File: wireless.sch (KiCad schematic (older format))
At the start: 18 parts, among them U7 NRF24L01+, X2 16MHz 10ppm

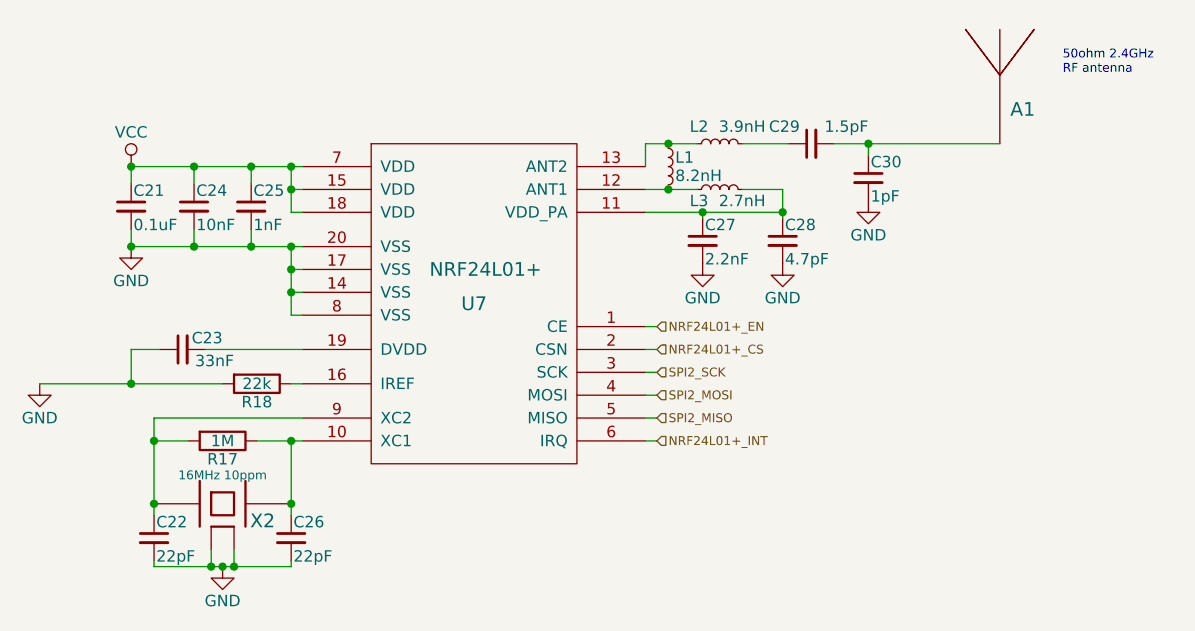
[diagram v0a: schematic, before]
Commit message: Fix problems noted by @nuft during review
- Force pulldown on unused bootloadr pins (USART 1 & 3)
- Use one oscillator for both MCU and NRF
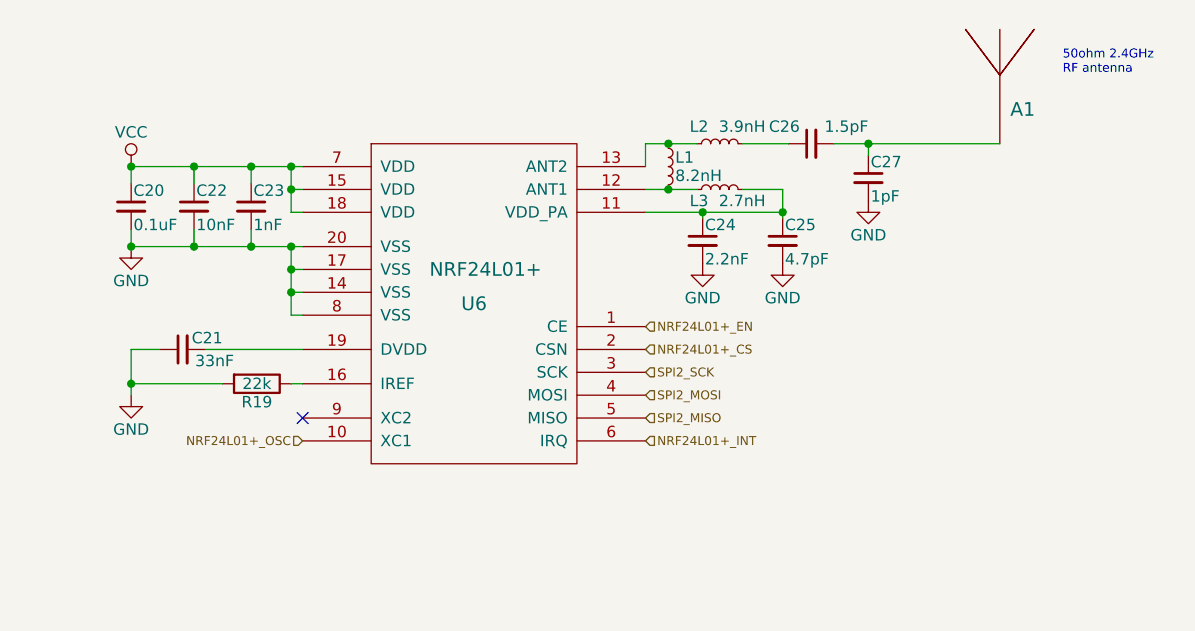
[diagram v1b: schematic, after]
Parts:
- removed C22, C26: 22pF, _std:_0402, symbol C_Small
- removed R17: 1M, _std:_0402, symbol R
- removed X2: 16MHz 10ppm, _div:_TSX-3225-SMD-XTAL, symbol XTAL-SMD-4-PADS
- renumbered C21 to C20, C23 to C21, C24 to C22, C25 to C23, C27 to C24, C28 to C25, C29 to C26, C30 to C27, R18 to R19, U7 to U6
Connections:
- net NRF24L01+_OSC: now reaches U6.10 (XC1)
- no-connect marks 0 -> 1
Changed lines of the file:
@@
 Sheet 3 4
 Title "Speedy the nanocopter"
-Date "2016-02-01"
+Date "2016-02-19"
 Rev "1C"
 Comp "Salah-Eddine Missri"
@@
 $EndDescr
 $Comp
-L NRF24R01+ U7
+L NRF24R01+ U6
 U 1 1 55438B0D
 P 5175 3125
-F 0 "U7" H 5175 3125 60  0000 C CNN
+F 0 "U6" H 5175 3125 60  0000 C CNN
 F 1 "NRF24L01+" H 5225 3275 60  0000 C CNN
 F 2 "Housings_DFN_QFN:QFN-20-1EP_4x4mm_Pitch0.5mm" H 5175 3125 60  0001 C CNN
@@
 $EndComp
 $Comp
-L VCC #PWR041
+L VCC #PWR036
 U 1 1 55438B1A
 P 3675 2525
-F 0 "#PWR041" H 3675 2375 50  0001 C CNN
+F 0 "#PWR036" H 3675 2375 50  0001 C CNN
 F 1 "VCC" H 3675 2675 50  0000 C CNN
 F 2 "" H 3675 2525 60  0000 C CNN
@@
 $EndComp
 $Comp
-L GND #PWR042
+L GND #PWR037
 U 1 1 55438B20
-P 3275 3475
-F 0 "#PWR042" H 3275 3225 50  0001 C CNN
-F 1 "GND" H 3275 3325 50  0000 C CNN
-F 2 "" H 3275 3475 60  0000 C CNN
-F 3 "" H 3275 3475 60  0000 C CNN
-	1    3275 3475
-	1    0    0    -1
-$EndComp
-$Comp
-L R R18
+P 3675 3525
+F 0 "#PWR037" H 3675 3275 50  0001 C CNN
+F 1 "GND" H 3675 3375 50  0000 C CNN
+F 2 "" H 3675 3525 60  0000 C CNN
+F 3 "" H 3675 3525 60  0000 C CNN
+	1    3675 3525
+	1    0    0    -1
+$EndComp
+$Comp
+L R R19
 U 1 1 55438B26
 P 4225 3475
-F 0 "R18" V 4305 3475 50  0000 C CNN
+F 0 "R19" V 4305 3475 50  0000 C CNN
 F 1 "22k" V 4225 3475 50  0000 C CNN
 F 2 "_std:_0402" V 4155 3475 30  0001 C CNN
@@
 $EndComp
 $Comp
-L GND #PWR043
-U 1 1 55438B2D
-P 4075 4275
-F 0 "#PWR043" H 4075 4025 50  0001 C CNN
-F 1 "GND" H 4075 4125 50  0000 C CNN
-F 2 "" H 4075 4275 60  0000 C CNN
-F 3 "" H 4075 4275 60  0000 C CNN
-	1    4075 4275
-	1    0    0    -1
-$EndComp
-$Comp
-L GND #PWR044
+L GND #PWR038
 U 1 1 55438B33
 P 6175 2950
-F 0 "#PWR044" H 6175 2700 50  0001 C CNN
+F 0 "#PWR038" H 6175 2700 50  0001 C CNN
 F 1 "GND" H 6175 2800 50  0000 C CNN
 F 2 "" H 6175 2950 60  0000 C CNN
@@
 $EndComp
 $Comp
-L GND #PWR045
+L GND #PWR039
 U 1 1 55438B39
 P 6525 2950
-F 0 "#PWR045" H 6525 2700 50  0001 C CNN
+F 0 "#PWR039" H 6525 2700 50  0001 C CNN
 F 1 "GND" H 6525 2800 50  0000 C CNN
 F 2 "" H 6525 2950 60  0000 C CNN
@@
 $EndComp
 $Comp
-L C_Small C29
+L C_Small C26
 U 1 1 55438B54
 P 6650 2425
-F 0 "C29" V 6725 2475 50  0000 L CNN
+F 0 "C26" V 6725 2475 50  0000 L CNN
 F 1 "1.5pF" V 6725 2175 50  0000 L CNN
 F 2 "_std:_0402" H 6650 2425 60  0001 C CNN
@@
 $EndComp
 $Comp
-L GND #PWR046
+L GND #PWR040
 U 1 1 55438B5B
 P 6900 2675
-F 0 "#PWR046" H 6900 2425 50  0001 C CNN
+F 0 "#PWR040" H 6900 2425 50  0001 C CNN
 F 1 "GND" H 6900 2525 50  0000 C CNN
 F 2 "" H 6900 2675 60  0000 C CNN
@@
 $EndComp
 $Comp
-L C_Small C27
+L C_Small C24
 U 1 1 55438B61
 P 6175 2850
-F 0 "C27" H 6185 2920 50  0000 L CNN
+F 0 "C24" H 6185 2920 50  0000 L CNN
 F 1 "2.2nF" H 6185 2770 50  0000 L CNN
 F 2 "_std:_0402" H 6175 2850 60  0001 C CNN
@@
 $EndComp
 $Comp
-L C_Small C28
+L C_Small C25
 U 1 1 55438B68
 P 6525 2850
-F 0 "C28" H 6535 2920 50  0000 L CNN
+F 0 "C25" H 6535 2920 50  0000 L CNN
 F 1 "4.7pF" H 6535 2770 50  0000 L CNN
 F 2 "_std:_0402" H 6525 2850 60  0001 C CNN
@@
 $EndComp
 $Comp
-L R R17
-U 1 1 55438B76
-P 4075 3725
-F 0 "R17" V 4155 3725 50  0000 C CNN
-F 1 "1M" V 4075 3725 50  0000 C CNN
-F 2 "_std:_0402" V 4005 3725 30  0001 C CNN
-F 3 "" H 4075 3725 30  0000 C CNN
-	1    4075 3725
-	0    1    1    0
-$EndComp
-$Comp
-L C_Small C22
-U 1 1 55438B7D
-P 3775 4150
-F 0 "C22" H 3785 4220 50  0000 L CNN
-F 1 "22pF" H 3785 4070 50  0000 L CNN
-F 2 "_std:_0402" H 3775 4150 60  0001 C CNN
-F 3 "" H 3775 4150 60  0000 C CNN
-	1    3775 4150
-	1    0    0    -1
-$EndComp
-$Comp
-L C_Small C26
-U 1 1 55438B84
-P 4375 4150
-F 0 "C26" H 4385 4220 50  0000 L CNN
-F 1 "22pF" H 4385 4070 50  0000 L CNN
-F 2 "_std:_0402" H 4375 4150 60  0001 C CNN
-F 3 "" H 4375 4150 60  0000 C CNN
-	1    4375 4150
-	1    0    0    -1
-$EndComp
-$Comp
-L C_Small C23
+L C_Small C21
 U 1 1 55438B8B
 P 3900 3325
-F 0 "C23" V 3950 3150 50  0000 L CNN
+F 0 "C21" V 3950 3150 50  0000 L CNN
 F 1 "33nF" V 3850 3100 50  0000 L CNN
 F 2 "_std:_0402" H 3900 3325 60  0001 C CNN
@@
 $EndComp
 $Comp
-L C_Small C30
+L C_Small C27
 U 1 1 55438B92
 P 6900 2575
-F 0 "C30" H 6910 2645 50  0000 L CNN
+F 0 "C27" H 6910 2645 50  0000 L CNN
 F 1 "1pF" H 6910 2495 50  0000 L CNN
 F 2 "_std:_0402" H 6900 2575 60  0001 C CNN
@@
 $EndComp
 $Comp
-L C_Small C21
+L C_Small C20
 U 1 1 55438B99
 P 3675 2700
-F 0 "C21" H 3685 2770 50  0000 L CNN
+F 0 "C20" H 3685 2770 50  0000 L CNN
 F 1 "0.1uF" H 3685 2620 50  0000 L CNN
 F 2 "_std:_0402" H 3675 2700 60  0001 C CNN
@@
 $EndComp
 $Comp
-L C_Small C25
+L C_Small C23
 U 1 1 55438BA0
 P 4200 2700
-F 0 "C25" H 4210 2770 50  0000 L CNN
+F 0 "C23" H 4210 2770 50  0000 L CNN
 F 1 "1nF" H 4210 2620 50  0000 L CNN
 F 2 "_std:_0402" H 4200 2700 60  0001 C CNN
@@
 $EndComp
 $Comp
-L GND #PWR047
+L GND #PWR041
 U 1 1 55438BA7
 P 3675 2875
-F 0 "#PWR047" H 3675 2625 50  0001 C CNN
+F 0 "#PWR041" H 3675 2625 50  0001 C CNN
 F 1 "GND" H 3675 2725 50  0000 C CNN
 F 2 "" H 3675 2875 60  0000 C CNN
@@
 	1    0    0    -1
 $EndComp
-Connection ~ 4075 4275
-Wire Wire Line
-	3775 4275 4375 4275
-Connection ~ 3775 4000
-Connection ~ 4375 4000
-Connection ~ 4375 3725
-Connection ~ 3775 3725
-Wire Wire Line
-	3925 3725 3775 3725
 Connection ~ 3675 3475
 Wire Wire Line
-	3275 3475 4075 3475
-Wire Wire Line
-	4425 3475 4375 3475
+	3675 3325 3675 3525
+Wire Wire Line
+	3675 3475 4075 3475
 Wire Wire Line
 	3675 3325 3800 3325
@@
 Wire Wire Line
 	3675 2800 3675 2875
-Wire Wire Line
-	3675 3325 3675 3475
 Connection ~ 4200 2525
 Wire Wire Line
@@
 Wire Wire Line
 	3675 2875 4425 2875
-Wire Wire Line
-	3775 3625 3775 4050
-Wire Wire Line
-	4425 3625 3775 3625
-Wire Wire Line
-	4375 3725 4375 4050
-Wire Wire Line
-	4225 3725 4425 3725
-Wire Wire Line
-	5975 3725 5925 3725
-Wire Wire Line
-	5975 3225 5925 3225
-Wire Wire Line
-	5925 3625 5975 3625
-Wire Wire Line
-	5975 3525 5925 3525
-Wire Wire Line
-	5925 3425 5975 3425
-Wire Wire Line
-	5975 3325 5925 3325
 Wire Wire Line
 	6525 2625 6525 2750
@@
 Connection ~ 6025 2425
 Connection ~ 6025 2625
-Wire Wire Line
-	3775 4250 3775 4275
-Wire Wire Line
-	4375 4275 4375 4250
 Connection ~ 3675 2875
 Connection ~ 4375 2875
@@
 Connection ~ 4200 2875
 $Comp
-L C_Small C24
+L C_Small C22
 U 1 1 55438BFC
 P 3950 2700
-F 0 "C24" H 3960 2770 50  0000 L CNN
+F 0 "C22" H 3960 2770 50  0000 L CNN
 F 1 "10nF" H 3960 2620 50  0000 L CNN
 F 2 "_std:_0402" H 3950 2700 60  0001 C CNN
@@
 Text Notes 7750 2125 0    39   ~ 0
 50ohm 2.4GHz\nRF antenna
-Text HLabel 5975 3225 2    39   Input ~ 0
+Text HLabel 5925 3225 2    39   Input ~ 0
 NRF24L01+_EN
-Text HLabel 5975 3325 2    39   Input ~ 0
+Text HLabel 5925 3325 2    39   Input ~ 0
 NRF24L01+_CS
-Text HLabel 5975 3425 2    39   Input ~ 0
+Text HLabel 5925 3425 2    39   Input ~ 0
 SPI2_SCK
-Text HLabel 5975 3525 2    39   Input ~ 0
+Text HLabel 5925 3525 2    39   Input ~ 0
 SPI2_MOSI
-Text HLabel 5975 3625 2    39   Input ~ 0
+Text HLabel 5925 3625 2    39   Input ~ 0
 SPI2_MISO
-Text HLabel 5975 3725 2    39   Input ~ 0
+Text HLabel 5925 3725 2    39   Input ~ 0
 NRF24L01+_INT
-$Comp
-L XTAL-SMD-4-PADS X2
-U 1 1 558EB9B5
-P 4075 4000
-F 0 "X2" H 4250 3925 60  0000 C CNN
-F 1 "16MHz 10ppm" H 4075 4125 39  0000 C CNN
-F 2 "_div:_TSX-3225-SMD-XTAL" H 4075 4000 60  0001 C CNN
-F 3 "" H 4075 4000 60  0000 C CNN
-	1    4075 4000
-	1    0    0    -1
-$EndComp
-Wire Wire Line
-	4025 4200 4025 4275
-Connection ~ 4025 4275
-Wire Wire Line
-	4125 4200 4125 4275
-Connection ~ 4125 4275
+NoConn ~ 4425 3625
+Text HLabel 4425 3725 0    39   Input ~ 0
+NRF24L01+_OSC
+Wire Wire Line
+	4425 3475 4375 3475
 $EndSCHEMATC

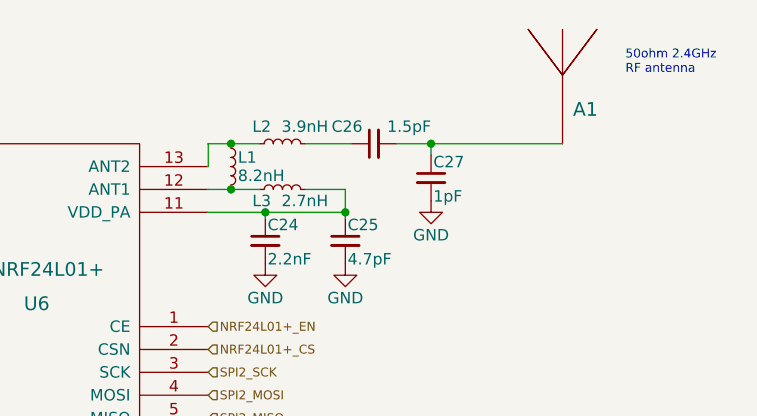
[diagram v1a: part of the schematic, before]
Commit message: Update TOF sensor to use new ST VL53L0X with 2m range
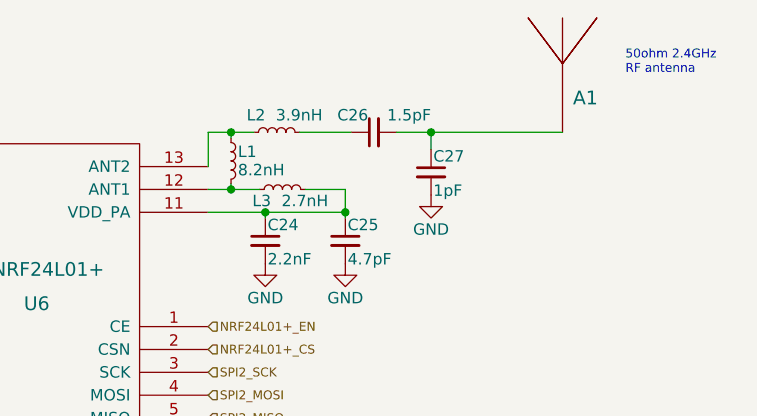
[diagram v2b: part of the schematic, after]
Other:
- moved on the sheet: A1, C26, C27, L1, L2
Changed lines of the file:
@@
 $EndComp
 $Comp
-L VCC #PWR036
+L VCC #PWR035
 U 1 1 55438B1A
 P 3675 2525
-F 0 "#PWR036" H 3675 2375 50  0001 C CNN
+F 0 "#PWR035" H 3675 2375 50  0001 C CNN
 F 1 "VCC" H 3675 2675 50  0000 C CNN
 F 2 "" H 3675 2525 60  0000 C CNN
@@
 $EndComp
 $Comp
-L GND #PWR037
+L GND #PWR036
 U 1 1 55438B20
 P 3675 3525
-F 0 "#PWR037" H 3675 3275 50  0001 C CNN
+F 0 "#PWR036" H 3675 3275 50  0001 C CNN
 F 1 "GND" H 3675 3375 50  0000 C CNN
 F 2 "" H 3675 3525 60  0000 C CNN
@@
 $EndComp
 $Comp
-L GND #PWR038
+L GND #PWR037
 U 1 1 55438B33
 P 6175 2950
-F 0 "#PWR038" H 6175 2700 50  0001 C CNN
+F 0 "#PWR037" H 6175 2700 50  0001 C CNN
 F 1 "GND" H 6175 2800 50  0000 C CNN
 F 2 "" H 6175 2950 60  0000 C CNN
@@
 $EndComp
 $Comp
-L GND #PWR039
+L GND #PWR038
 U 1 1 55438B39
 P 6525 2950
-F 0 "#PWR039" H 6525 2700 50  0001 C CNN
+F 0 "#PWR038" H 6525 2700 50  0001 C CNN
 F 1 "GND" H 6525 2800 50  0000 C CNN
 F 2 "" H 6525 2950 60  0000 C CNN
@@
 L L_Small L1
 U 1 1 55438B3F
-P 6025 2525
-F 0 "L1" H 6055 2565 50  0000 L CNN
-F 1 "8.2nH" H 6055 2485 50  0000 L CNN
-F 2 "_std:_0402" H 6025 2525 60  0001 C CNN
-F 3 "" H 6025 2525 60  0000 C CNN
-	1    6025 2525
+P 6025 2500
+F 0 "L1" H 6055 2540 50  0000 L CNN
+F 1 "8.2nH" H 6055 2460 50  0000 L CNN
+F 2 "_std:_0402" H 6025 2500 60  0001 C CNN
+F 3 "" H 6025 2500 60  0000 C CNN
+	1    6025 2500
 	1    0    0    -1
 $EndComp
@@
 L L_Small L2
 U 1 1 55438B46
-P 6250 2425
-F 0 "L2" V 6325 2475 50  0000 L CNN
-F 1 "3.9nH" V 6325 2225 50  0000 L CNN
-F 2 "_std:_0402" H 6250 2425 60  0001 C CNN
-F 3 "" H 6250 2425 60  0000 C CNN
-	1    6250 2425
+P 6225 2375
+F 0 "L2" V 6300 2425 50  0000 L CNN
+F 1 "3.9nH" V 6300 2175 50  0000 L CNN
+F 2 "_std:_0402" H 6225 2375 60  0001 C CNN
+F 3 "" H 6225 2375 60  0000 C CNN
+	1    6225 2375
 	0    -1   -1   0
 $EndComp
@@
 L C_Small C26
 U 1 1 55438B54
-P 6650 2425
-F 0 "C26" V 6725 2475 50  0000 L CNN
-F 1 "1.5pF" V 6725 2175 50  0000 L CNN
-F 2 "_std:_0402" H 6650 2425 60  0001 C CNN
-F 3 "" H 6650 2425 60  0000 C CNN
-	1    6650 2425
+P 6650 2375
+F 0 "C26" V 6725 2400 50  0000 L CNN
+F 1 "1.5pF" V 6725 2125 50  0000 L CNN
+F 2 "_std:_0402" H 6650 2375 60  0001 C CNN
+F 3 "" H 6650 2375 60  0000 C CNN
+	1    6650 2375
 	0    -1   -1   0
 $EndComp
 $Comp
-L GND #PWR040
+L GND #PWR039
 U 1 1 55438B5B
-P 6900 2675
-F 0 "#PWR040" H 6900 2425 50  0001 C CNN
-F 1 "GND" H 6900 2525 50  0000 C CNN
-F 2 "" H 6900 2675 60  0000 C CNN
-F 3 "" H 6900 2675 60  0000 C CNN
-	1    6900 2675
+P 6900 2650
+F 0 "#PWR039" H 6900 2400 50  0001 C CNN
+F 1 "GND" H 6900 2500 50  0000 C CNN
+F 2 "" H 6900 2650 60  0000 C CNN
+F 3 "" H 6900 2650 60  0000 C CNN
+	1    6900 2650
 	1    0    0    -1
 $EndComp
@@
 L C_Small C27
 U 1 1 55438B92
-P 6900 2575
-F 0 "C27" H 6910 2645 50  0000 L CNN
-F 1 "1pF" H 6910 2495 50  0000 L CNN
-F 2 "_std:_0402" H 6900 2575 60  0001 C CNN
-F 3 "" H 6900 2575 60  0000 C CNN
-	1    6900 2575
+P 6900 2550
+F 0 "C27" H 6910 2620 50  0000 L CNN
+F 1 "1pF" H 6910 2470 50  0000 L CNN
+F 2 "_std:_0402" H 6900 2550 60  0001 C CNN
+F 3 "" H 6900 2550 60  0000 C CNN
+	1    6900 2550
 	1    0    0    -1
 $EndComp
@@
 $EndComp
 $Comp
-L GND #PWR041
+L GND #PWR040
 U 1 1 55438BA7
 P 3675 2875
-F 0 "#PWR041" H 3675 2625 50  0001 C CNN
+F 0 "#PWR040" H 3675 2625 50  0001 C CNN
 F 1 "GND" H 3675 2725 50  0000 C CNN
 F 2 "" H 3675 2875 60  0000 C CNN
@@
 	5925 2625 6150 2625
 Wire Wire Line
-	5925 2425 6150 2425
+	5925 2375 6125 2375
 Wire Wire Line
 	6350 2625 6525 2625
 Connection ~ 6525 2725
 Wire Wire Line
-	6550 2425 6350 2425
-Wire Wire Line
-	5925 2425 5925 2525
-Connection ~ 6025 2425
-Connection ~ 6025 2625
+	6550 2375 6325 2375
+Wire Wire Line
+	5925 2375 5925 2525
 Connection ~ 3675 2875
 Connection ~ 4375 2875
@@
 L ANTENNA A1
 U 1 1 55438C07
-P 7475 2125
-F 0 "A1" H 7575 1975 60  0000 C CNN
-F 1 "ANTENNA" H 7475 2425 60  0001 C CNN
-F 2 "_div:_ANT-2.45-CHP" H 7475 2125 60  0001 C CNN
-F 3 "" H 7475 2125 60  0000 C CNN
-	1    7475 2125
-	1    0    0    -1
-$EndComp
-Wire Wire Line
-	6900 2475 6900 2425
-Wire Wire Line
-	6750 2425 7475 2425
-Connection ~ 6900 2425
+P 7475 2075
+F 0 "A1" H 7575 1925 60  0000 C CNN
+F 1 "ANTENNA" H 7475 2375 60  0001 C CNN
+F 2 "_div:_ANT-2.45-CHP" H 7475 2075 60  0001 C CNN
+F 3 "" H 7475 2075 60  0000 C CNN
+	1    7475 2075
+	1    0    0    -1
+$EndComp
+Wire Wire Line
+	6900 2450 6900 2375
+Wire Wire Line
+	6750 2375 7475 2375
+Connection ~ 6900 2375
 Text Notes 7750 2125 0    39   ~ 0
 50ohm 2.4GHz\nRF antenna
@@
 Wire Wire Line
 	4425 3475 4375 3475
+Wire Wire Line
+	6025 2400 6025 2375
+Connection ~ 6025 2375
+Wire Wire Line
+	6025 2600 6025 2625
+Connection ~ 6025 2625
 $EndSCHEMATC
